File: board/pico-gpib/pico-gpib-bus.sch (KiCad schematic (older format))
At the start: 32 parts, among them J1 GPIB, U2 SN75160BDW, U3 SN75162BDW, U6 NCP1117-2.5

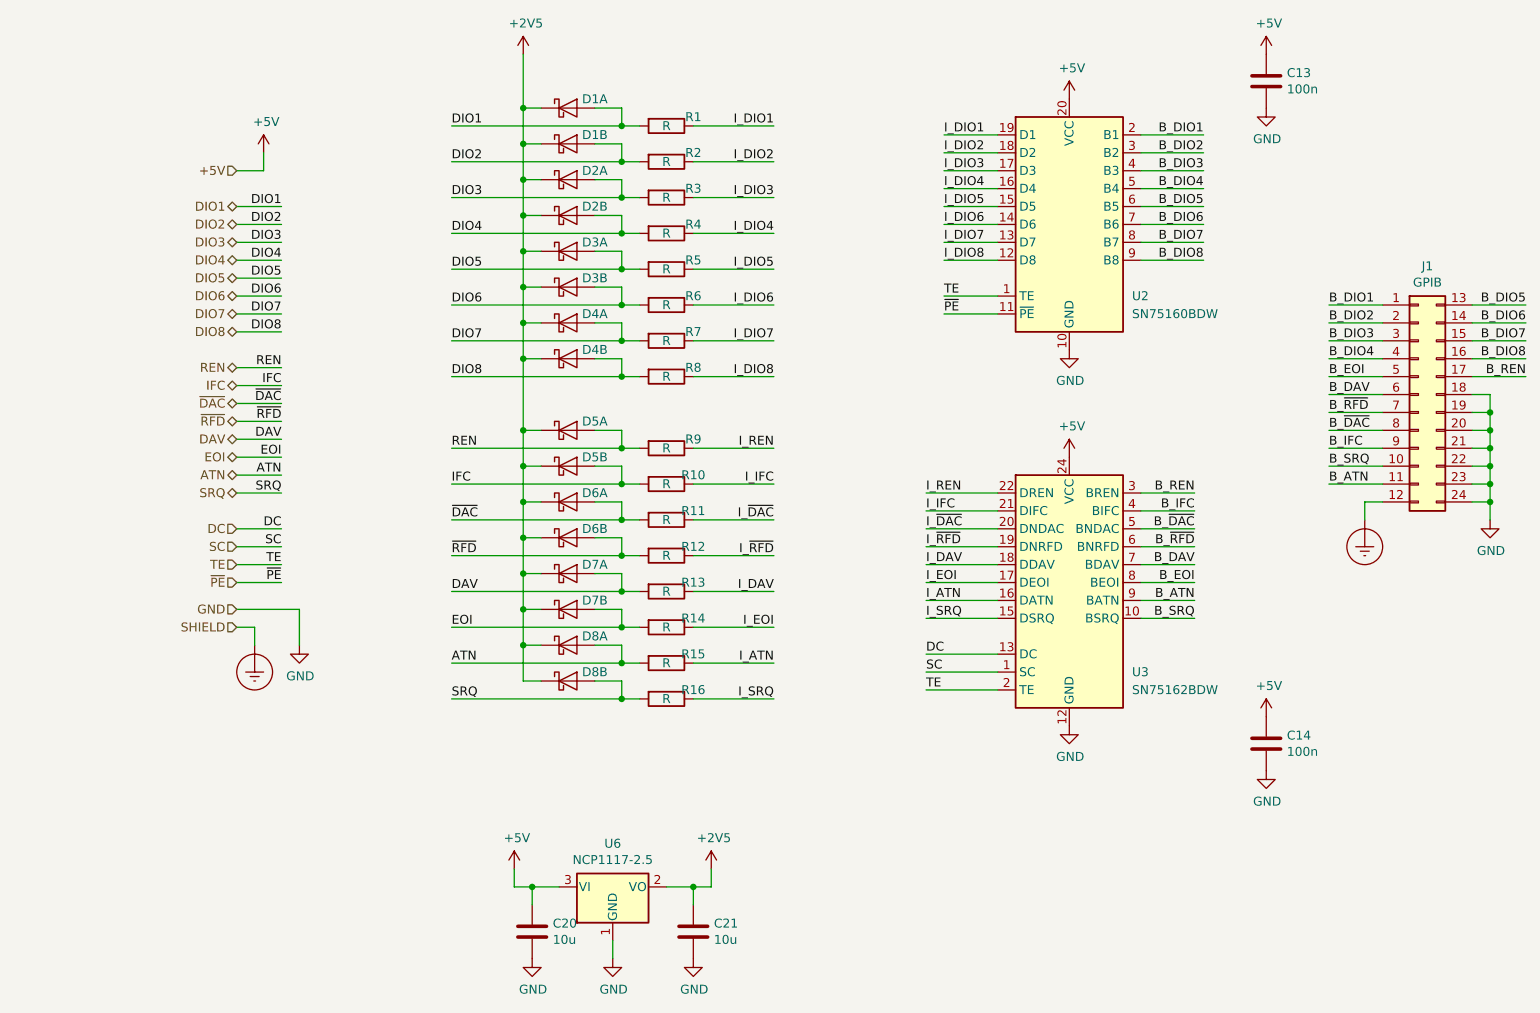
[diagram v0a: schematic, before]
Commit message: Rotate RP2040 to fit in crystal.
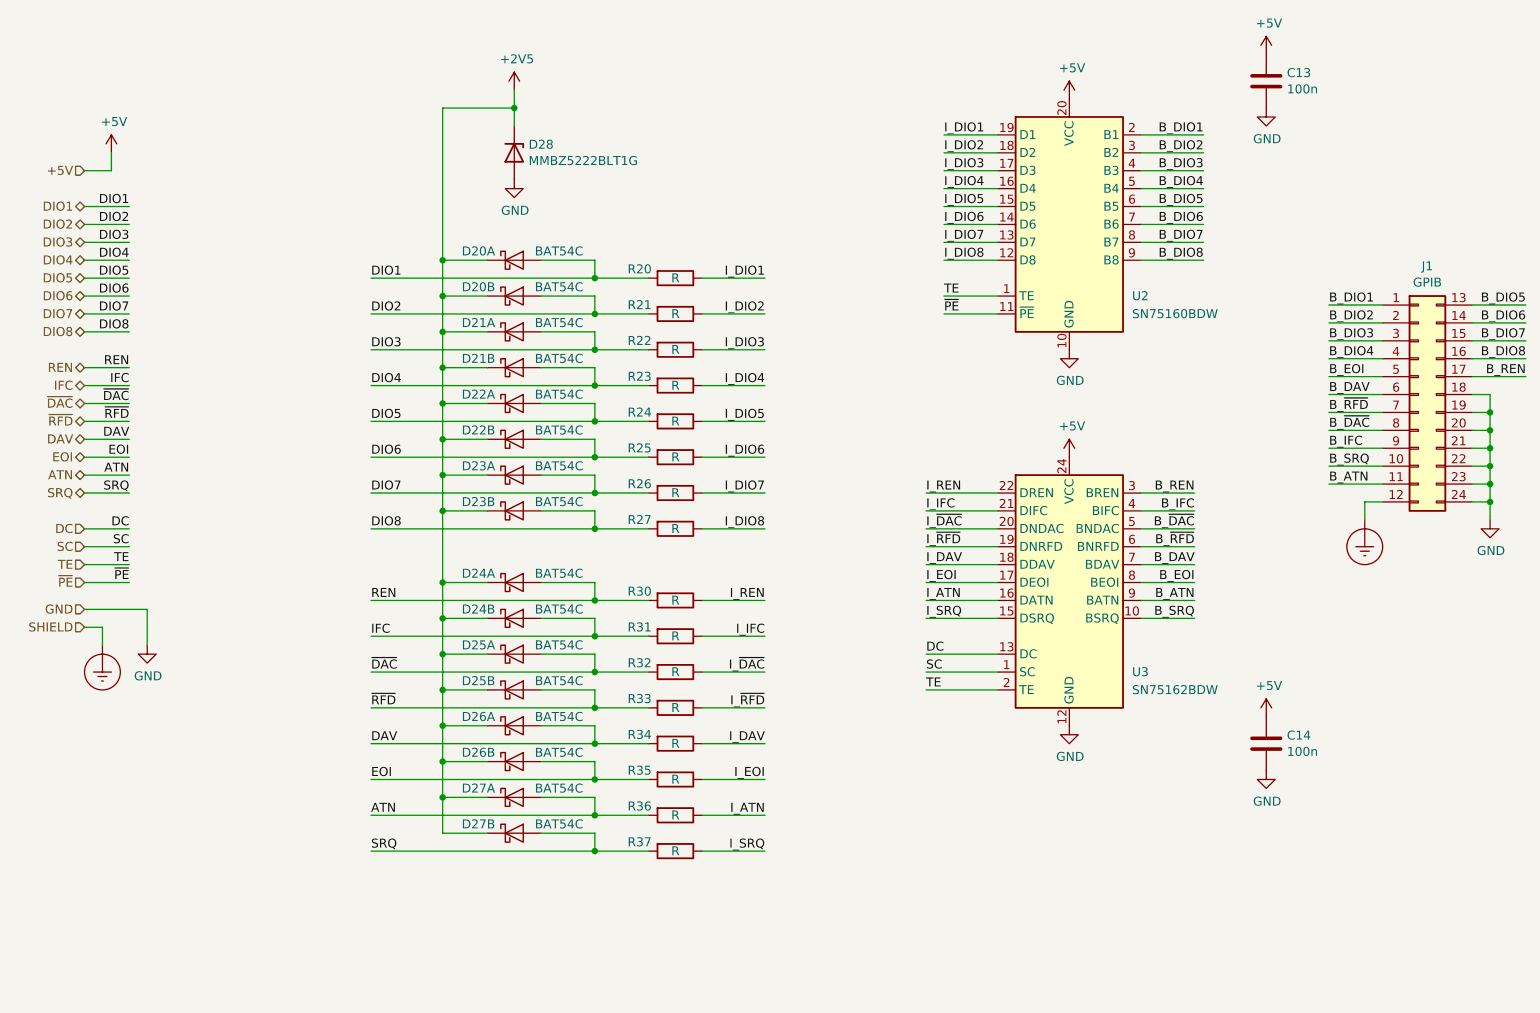
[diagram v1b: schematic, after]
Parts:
- removed C20, C21: 10u, Capacitor_SMD:C_0402_1005Metric, symbol Device:C
- removed U6: NCP1117-2.5, Package_TO_SOT_SMD:SOT-223-3_TabPin2, symbol Regulator_Linear:NCP1117-2.5_SOT223
- added D28: MMBZ5222BLT1G, Package_TO_SOT_SMD:SC-59, symbol Device:D_Zener
- D20: renamed from D1; value D_Schottky_x2_KCom_AAK_Split -> BAT54C
- D21: renamed from D2; value D_Schottky_x2_KCom_AAK_Split -> BAT54C
- D22: renamed from D3; value D_Schottky_x2_KCom_AAK_Split -> BAT54C
- D23: renamed from D4; value D_Schottky_x2_KCom_AAK_Split -> BAT54C
- D24: renamed from D5; value D_Schottky_x2_KCom_AAK_Split -> BAT54C
- D25: renamed from D6; value D_Schottky_x2_KCom_AAK_Split -> BAT54C
- D26: renamed from D7; value D_Schottky_x2_KCom_AAK_Split -> BAT54C
- D27: renamed from D8; value D_Schottky_x2_KCom_AAK_Split -> BAT54C
- renumbered R1 to R20, R2 to R21, R3 to R22, R4 to R23, R5 to R24, R6 to R25, R7 to R26, R8 to R27, R9 to R30, R10 to R31, R11 to R32, R12 to R33, R13 to R34, R14 to R35, R15 to R36, R16 to R37
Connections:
- net +2V5: now also D28.3 (K)
- net GND: now also D28.1 (A)
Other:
- moved on the sheet: D20A, D20B, D21A, D21B, D22A, D22B, D23A, D23B, D24A, D24B, D25A, D25B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

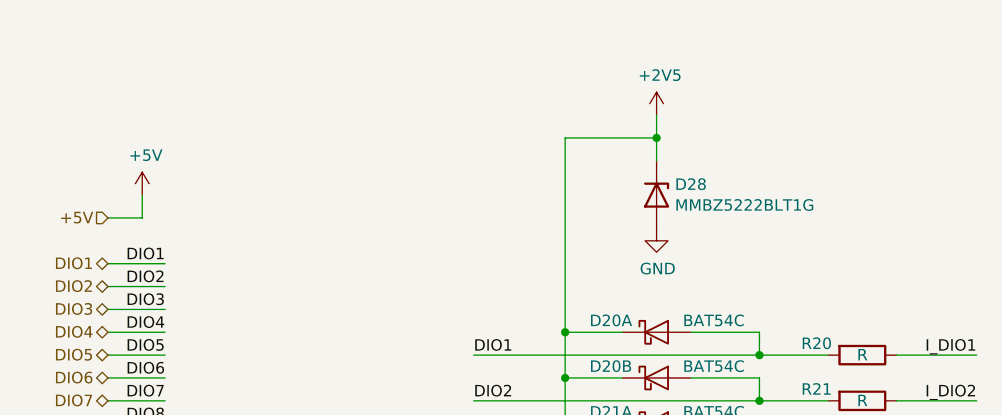
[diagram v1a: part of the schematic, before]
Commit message: Add labels and test points.
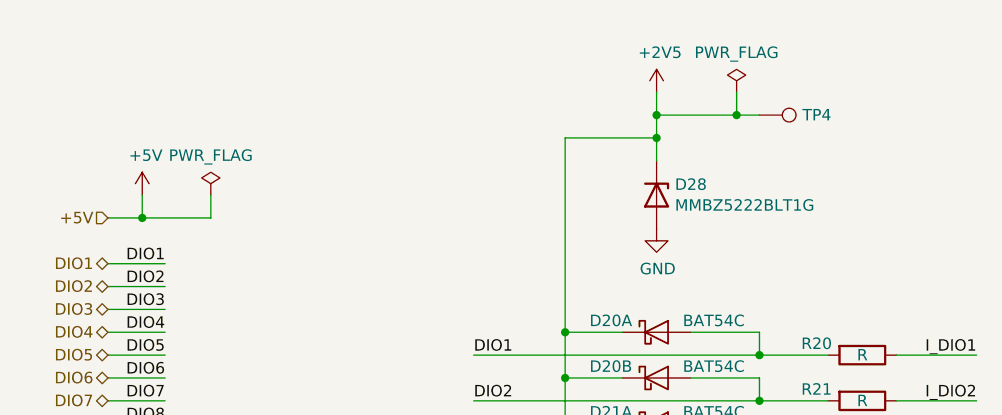
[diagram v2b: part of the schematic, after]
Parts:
- added TP4: TestPoint, TestPoint:TestPoint_Pad_D1.0mm, symbol Connector:TestPoint
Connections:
- net +2V5: now also TP4.1
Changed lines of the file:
@@
 L power:+2V5 #PWR0130
 U 1 1 62E7D72C
-P 3900 1550
-F 0 "#PWR0130" H 3900 1400 50  0001 C CNN
-F 1 "+2V5" H 3915 1723 50  0000 C CNN
-F 2 "" H 3900 1550 50  0001 C CNN
-F 3 "" H 3900 1550 50  0001 C CNN
-	1    3900 1550
+P 3900 1450
+F 0 "#PWR0130" H 3900 1300 50  0001 C CNN
+F 1 "+2V5" H 3915 1623 50  0000 C CNN
+F 2 "" H 3900 1450 50  0001 C CNN
+F 3 "" H 3900 1450 50  0001 C CNN
+	1    3900 1450
 	1    0    0    -1
 $EndComp
+$Comp
+L power:PWR_FLAG #FLG0101
+U 1 1 6377C655
+P 1950 1900
+F 0 "#FLG0101" H 1950 1975 50  0001 C CNN
+F 1 "PWR_FLAG" H 1950 2073 50  0000 C CNN
+F 2 "" H 1950 1900 50  0001 C CNN
+F 3 "~" H 1950 1900 50  0001 C CNN
+	1    1950 1900
+	1    0    0    -1
+$EndComp
+$Comp
+L power:PWR_FLAG #FLG0102
+U 1 1 6377CB2C
+P 4250 1450
+F 0 "#FLG0102" H 4250 1525 50  0001 C CNN
+F 1 "PWR_FLAG" H 4250 1623 50  0000 C CNN
+F 2 "" H 4250 1450 50  0001 C CNN
+F 3 "~" H 4250 1450 50  0001 C CNN
+	1    4250 1450
+	1    0    0    -1
+$EndComp
+Wire Wire Line
+	1650 2000 1950 2000
+Wire Wire Line
+	1950 2000 1950 1900
+Connection ~ 1650 2000
+Wire Wire Line
+	3900 1550 4250 1550
+Wire Wire Line
+	4250 1550 4250 1450
+Connection ~ 3900 1550
+Wire Wire Line
+	3900 1550 3900 1450
+$Comp
+L Connector:TestPoint TP4
+U 1 1 637C8F2D
+P 4350 1550
+F 0 "TP4" V 4350 1738 50  0000 L CNN
+F 1 "TestPoint" V 4395 1738 50  0001 L CNN
+F 2 "TestPoint:TestPoint_Pad_D1.0mm" H 4550 1550 50  0001 C CNN
+F 3 "~" H 4550 1550 50  0001 C CNN
+	1    4350 1550
+	0    1    1    0
+$EndComp
+Wire Wire Line
+	4250 1550 4350 1550
+Connection ~ 4250 1550
 $EndSCHEMATC

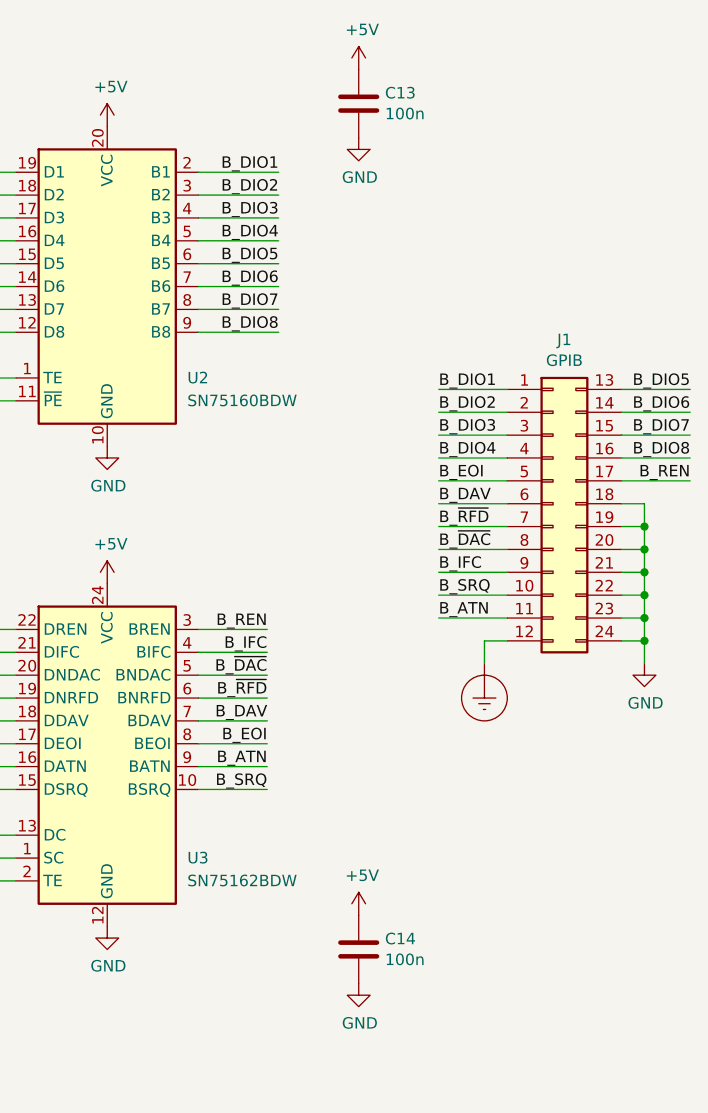
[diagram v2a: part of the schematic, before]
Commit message: Renumber caps to make more sense.
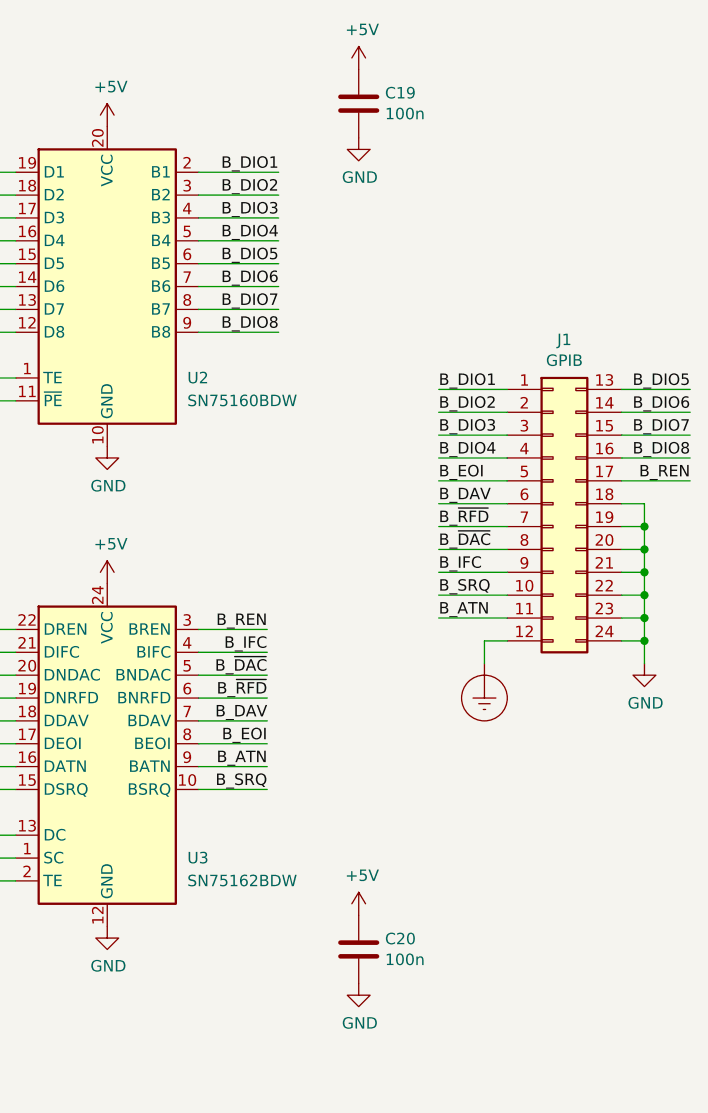
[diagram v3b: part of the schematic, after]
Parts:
- renumbered C13 to C19, C14 to C20
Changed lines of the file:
@@
 P 8100 1500
 AR Path="/62857BC0" Ref="C?"  Part="1"
-AR Path="/62065D04/62857BC0" Ref="C13"  Part="1"
-F 0 "C13" H 8215 1546 50  0000 L CNN
+AR Path="/62065D04/62857BC0" Ref="C19"  Part="1"
+F 0 "C19" H 8215 1546 50  0000 L CNN
 F 1 "100n" H 8215 1455 50  0000 L CNN
 F 2 "Capacitor_SMD:C_0402_1005Metric" H 8138 1350 50  0001 C CNN
@@
 P 8100 5200
 AR Path="/6286CEF1" Ref="C?"  Part="1"
-AR Path="/62065D04/6286CEF1" Ref="C14"  Part="1"
-F 0 "C14" H 8215 5246 50  0000 L CNN
+AR Path="/62065D04/6286CEF1" Ref="C20"  Part="1"
+F 0 "C20" H 8215 5246 50  0000 L CNN
 F 1 "100n" H 8215 5155 50  0000 L CNN
 F 2 "Capacitor_SMD:C_0402_1005Metric" H 8138 5050 50  0001 C CNN

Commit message: Clean up pico schematic.
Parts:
- R20, R21, R22, R23, R24, R25, R26, R27, R30, R31, R32, R33, R34, R35, R36, R37: value R -> 1k
